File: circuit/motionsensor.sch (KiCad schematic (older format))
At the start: 12 parts, among them IC1 ATTINY85-P, K1 CONN_3, P1 CONN_2, P2 CONN_2, Q1 LOCAL_IRF540N, U1 7805

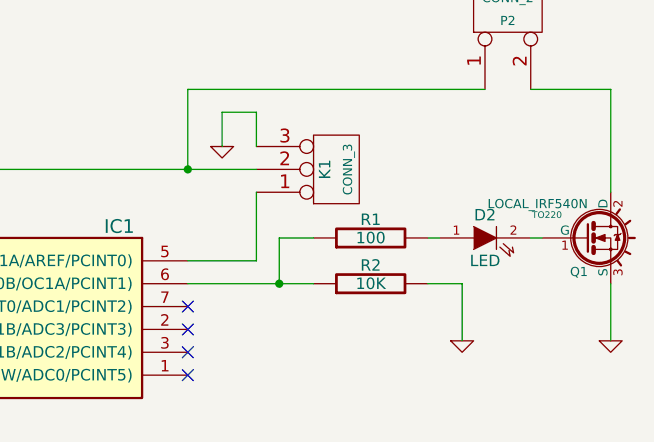
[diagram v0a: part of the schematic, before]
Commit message: Schematic update. Moved R1 and D2 to be in parallel with input to Q1 gate instead of in series.
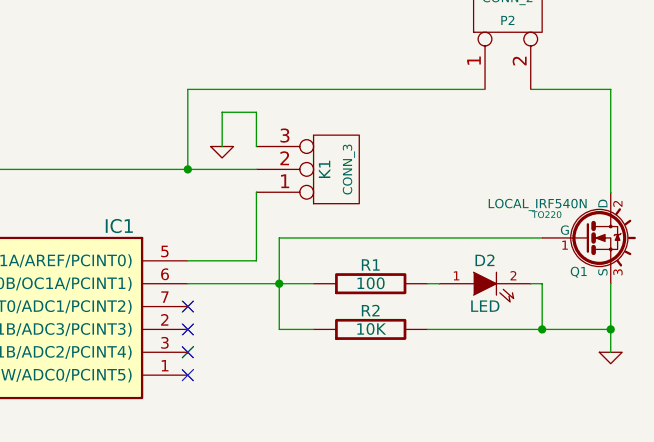
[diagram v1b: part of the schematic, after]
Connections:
- net GND: now also D2.2 (K)
- net at IC1.6 (PB1(MISO/DO/AIN1/OC0B/OC1A/PCINT1)), R1.1, R2.1: now also Q1.1 (G)
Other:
- moved on the sheet: D2, R1, R2
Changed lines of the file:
@@
-EESchema Schematic File Version 2  date Thu 06 Jun 2013 13:45:32 EST
+EESchema Schematic File Version 2  date Tue 02 Jul 2013 03:48:01 EST
 LIBS:power
 LIBS:device
@@
 LIBS:contrib
 LIBS:valves
-LIBS:localtransistors
 LIBS:motionsensor-cache
 EELAYER 25  0
@@
 Sheet 1 1
 Title "Motion-activated switch"
-Date "6 jun 2013"
+Date "1 jul 2013"
 Rev "0.1"
 Comp ""
@@
 $EndDescr
 Wire Wire Line
-	9300 3550 9350 3550
+	8200 3550 9350 3550
+Wire Wire Line
+	8200 3550 8200 3950
+Connection ~ 9650 3950
+Wire Wire Line
+	8850 3950 9650 3950
 Wire Wire Line
 	9650 3350 9650 2900
@@
 	3250 3250 3100 3250
 Wire Wire Line
-	9000 4000 9000 3750
-Wire Wire Line
-	9000 3750 8850 3750
-Wire Wire Line
-	8900 3550 8850 3550
+	8900 3750 8850 3750
 Wire Wire Line
 	7950 3150 7950 3000
@@
 	7800 2900 9100 2900
 Wire Wire Line
-	8350 3750 7800 3750
-Wire Wire Line
-	8350 3550 8200 3550
-Wire Wire Line
-	8200 3550 8200 3750
-Connection ~ 8200 3750
+	7800 3750 8350 3750
 Wire Wire Line
 	3650 3250 8100 3250
 Connection ~ 3800 3250
 Wire Wire Line
-	9650 3750 9650 4000
+	9650 3750 9650 4050
+Wire Wire Line
+	8200 3950 8350 3950
+Connection ~ 8200 3750
+Wire Wire Line
+	9300 3750 9350 3750
+Wire Wire Line
+	9350 3750 9350 3950
+Connection ~ 9350 3950
 $Comp
 L LOCAL_IRF540N Q1
@@
 $EndComp
 $Comp
-L GND #PWR6
-U 1 1 51AEBFA8
-P 9000 4000
-F 0 "#PWR6" H 9000 4000 30  0001 C CNN
-F 1 "GND" H 9000 3930 30  0001 C CNN
-	1    9000 4000
-	1    0    0    -1
-$EndComp
-$Comp
 L R R2
 U 1 1 51AEBF88
-P 8600 3750
-F 0 "R2" V 8680 3750 50  0000 C CNN
-F 1 "10K" V 8600 3750 50  0000 C CNN
-	1    8600 3750
+P 8600 3950
+F 0 "R2" V 8680 3950 50  0000 C CNN
+F 1 "10K" V 8600 3950 50  0000 C CNN
+	1    8600 3950
 	0    -1   -1   0
 $EndComp
@@
 L LED D2
 U 1 1 51AD811D
-P 9100 3550
-F 0 "D2" H 9100 3650 50  0000 C CNN
-F 1 "LED" H 9100 3450 50  0000 C CNN
-	1    9100 3550
+P 9100 3750
+F 0 "D2" H 9100 3850 50  0000 C CNN
+F 1 "LED" H 9100 3650 50  0000 C CNN
+	1    9100 3750
 	1    0    0    -1
 $EndComp
@@
 L GND #PWR7
 U 1 1 51A829DB
-P 9650 4000
-F 0 "#PWR7" H 9650 4000 30  0001 C CNN
-F 1 "GND" H 9650 3930 30  0001 C CNN
-	1    9650 4000
+P 9650 4050
+F 0 "#PWR7" H 9650 4050 30  0001 C CNN
+F 1 "GND" H 9650 3980 30  0001 C CNN
+	1    9650 4050
 	1    0    0    -1
 $EndComp
@@
 L R R1
 U 1 1 51A82807
-P 8600 3550
-F 0 "R1" V 8680 3550 50  0000 C CNN
-F 1 "100" V 8600 3550 50  0000 C CNN
-	1    8600 3550
+P 8600 3750
+F 0 "R1" V 8680 3750 50  0000 C CNN
+F 1 "100" V 8600 3750 50  0000 C CNN
+	1    8600 3750
 	0    -1   -1   0
 $EndComp
